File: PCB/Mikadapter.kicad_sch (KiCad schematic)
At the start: 10 parts, among them J1 FC68131, J3 FC68131, J4 FC68131, J5 Conn_01x02_Female, J6 Conn_01x03_Female, J7 Conn_01x02_Female, J8 Conn_01x04_Female, J9 Conn_01x03_Female

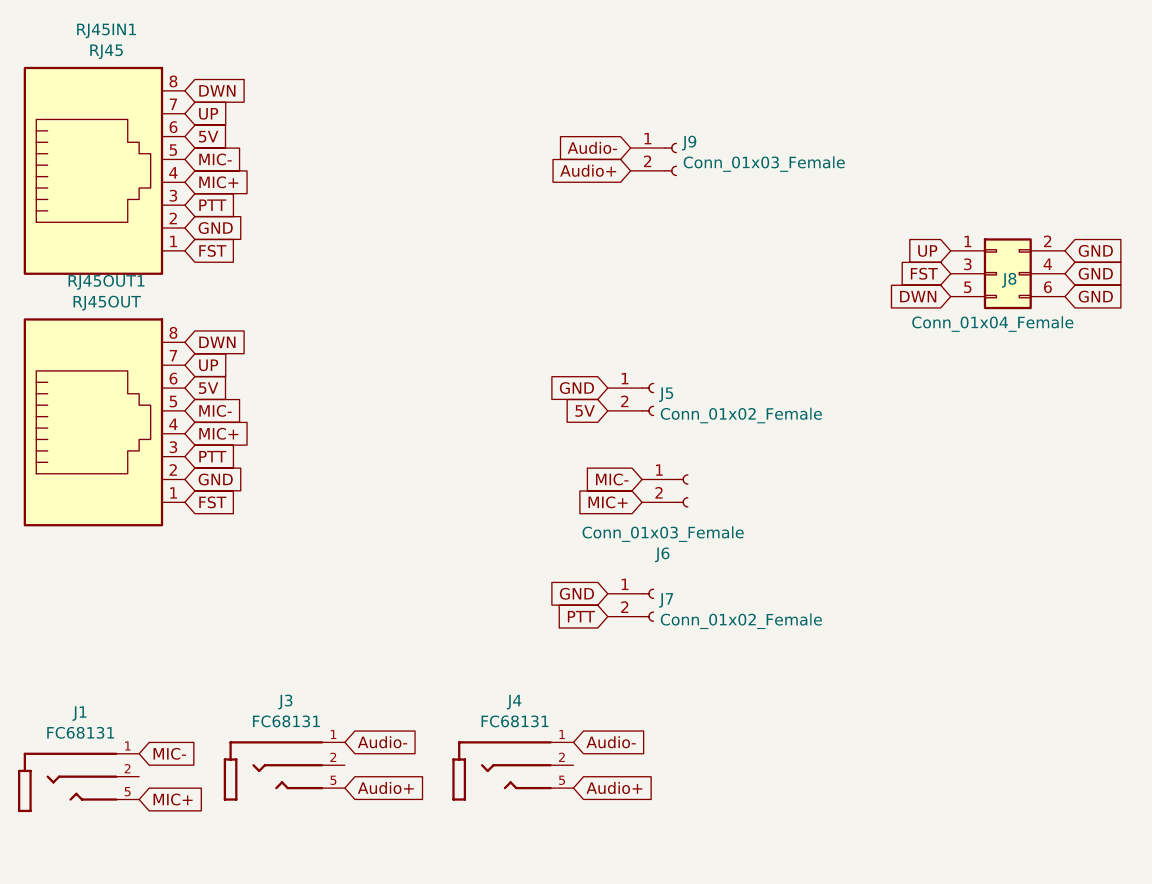
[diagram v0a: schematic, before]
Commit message: Added trace for second Audio channel, new folder, 3D
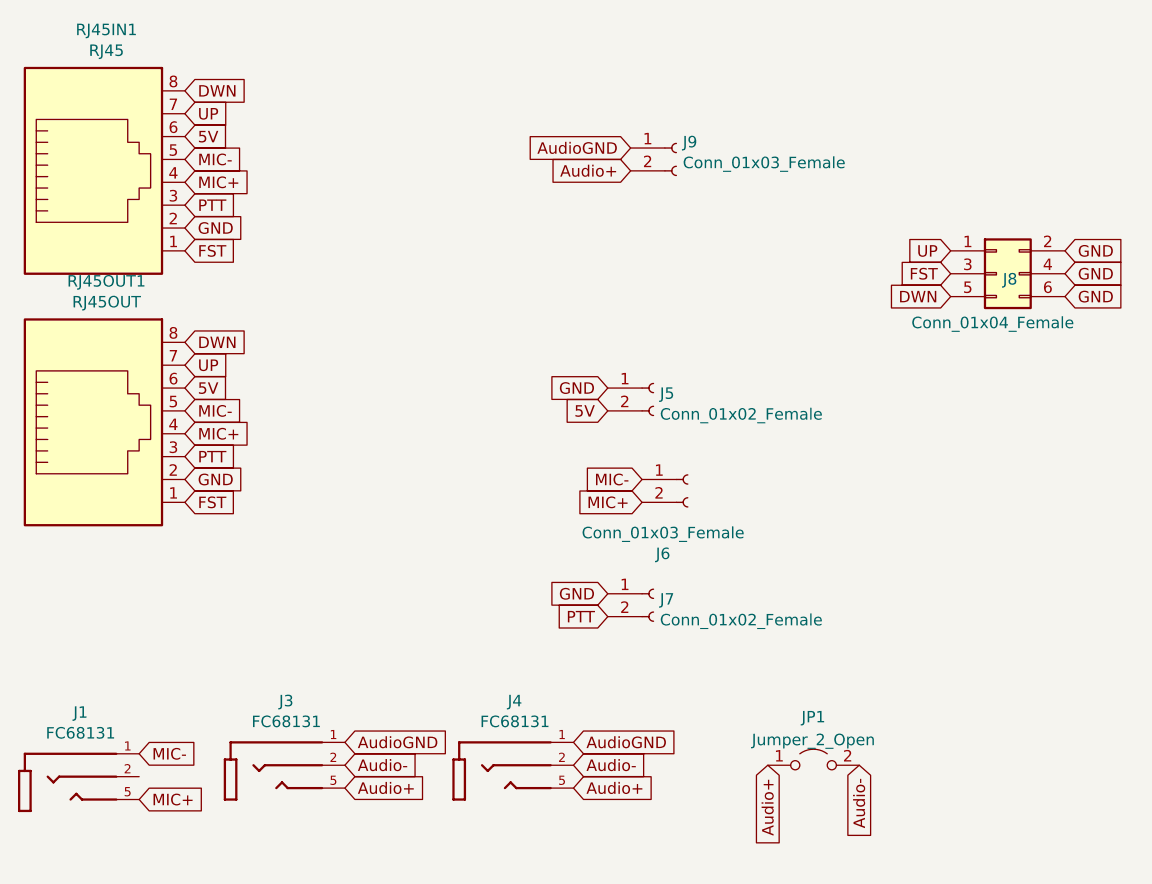
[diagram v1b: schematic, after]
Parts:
- added JP1: Jumper_2_Open, Jumper:SolderJumper-2_P1.3mm_Open_TrianglePad1.0x1.5mm, symbol Jumper:Jumper_2_Open
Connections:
- net Audio+: now also JP1.1 (A)
- net Audio-: now also J3.2, J4.2, JP1.2 (B); no longer J3.1, J4.1, J9.1 (Pin_1)
- new net AudioGND: J3.1, J4.1, J9.1 (Pin_1)
